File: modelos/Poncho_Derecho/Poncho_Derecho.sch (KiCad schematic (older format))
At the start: 5 parts, among them P1 CONN_4, P2 CONN_4

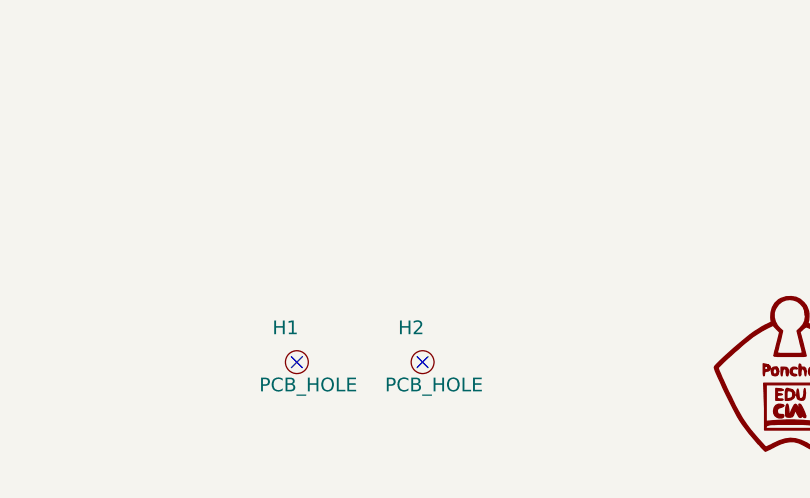
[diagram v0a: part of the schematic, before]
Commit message: * Unifico rótulos en los modelos.
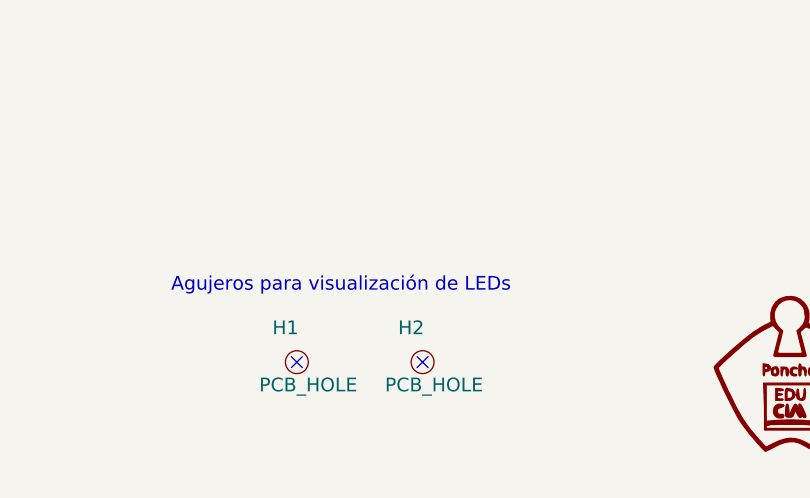
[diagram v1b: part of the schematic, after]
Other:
- note added: "Agujeros para visualización de LEDs"
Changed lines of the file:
@@
 Connection ~ 4000 2450
 NoConn ~ 4100 2050
+Text Notes 7450 5650 0    60   ~ 0
+Agujeros para visualización de LEDs
 $EndSCHEMATC
